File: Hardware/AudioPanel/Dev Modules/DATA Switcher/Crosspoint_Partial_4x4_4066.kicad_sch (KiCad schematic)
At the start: 29 parts, among them U1004 74HC4066BQ, U1005 74HC4066BQ, U1006 74HC4066BQ

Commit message: Many tweaks
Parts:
- removed C49, C50, C51, C53, C54, C55: 100nF, symbol Device:C_Small
- removed C52, C56: 10uF, symbol Device:C_Small
- added C901, C902, C903: 100nF, Capacitor_SMD:C_0402_1005Metric, symbol Device:C_Small
- added C904, C905: 22uF, Capacitor_SMD:C_0603_1608Metric, symbol Device:C_Small
- renumbered D1001 to D901, D1002 to D902, D1003 to D903, D1004 to D904, D1005 to D905, D1006 to D906, D1007 to D907, D1008 to D908, D1009 to D909, D210 to D910, D211 to D911, D212 to D912, RN201 to RN901, RN202 to RN902, RN203 to RN903, RN204 to RN904, RN205 to RN905, RN207 to RN906, U1004 to U901, U1005 to U902, U1006 to U903
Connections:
- net A1: now also D901.2 (A)
- net A1_T: no longer D901.2 (A)
- net A2: now also D902.2 (A)
- net A2_T: no longer D902.2 (A)
- net A3: now also D903.2 (A)
- net A3_T: no longer D903.2 (A)
- net B0: now also D904.2 (A)
- net B0_T: no longer D904.2 (A)
- net B2: now also D905.2 (A)
- net B2_T: no longer D905.2 (A)
- net B3: now also D906.2 (A)
- net B3_T: no longer D906.2 (A)
- net C0: now also D907.2 (A)
- net C0_T: no longer D907.2 (A)
- net C1: now also D908.2 (A)
- net C1_T: no longer D908.2 (A)
- net C3: now also D909.2 (A)
- net C3_T: no longer D909.2 (A)
- net D0: now also D910.2 (A)
- net D0_T: no longer D910.2 (A)
- net D1: now also D911.2 (A)
- net D1_T: no longer D911.2 (A)
- net D2: now also D912.2 (A)
- net D2_T: no longer D912.2 (A)
- net GND: now also C901.2, C902.2, C903.2, C904.2, C905.2
- net VDD: now also C901.1, C902.1, C903.1, C904.1, C905.1

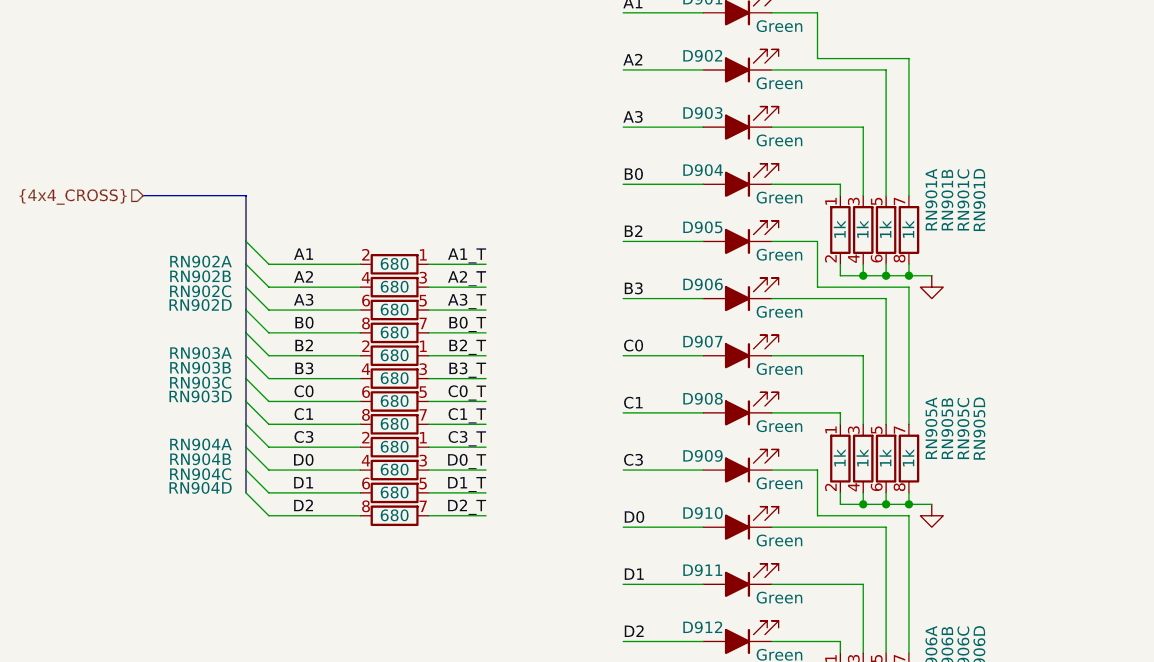
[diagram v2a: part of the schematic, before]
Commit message: Fixed value of RADIO SQUELCH low-pass filter cap
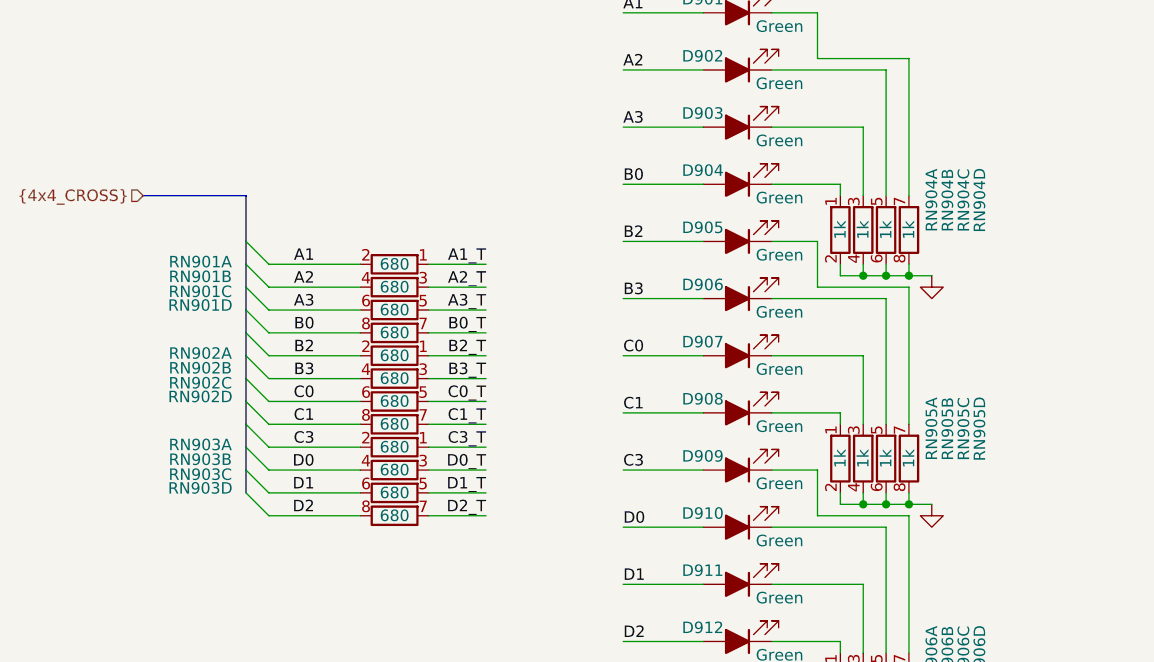
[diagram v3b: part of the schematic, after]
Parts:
- renumbered RN902 to RN901, RN903 to RN902, RN904 to RN903, RN901 to RN904
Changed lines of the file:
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@@
 		(on_board yes)
 		(dnp no)
-		(property "Reference" "RN904"
+		(property "Reference" "RN903"
 			(at 36.83 110.6057 90)
 			(effects
@@
 			(project "DATA Switcher"
 				(path "/f4364825-c4d0-42ed-9bb3-69baf38bc2d0/f5e12c3e-6416-4600-9203-1d5eae1952dd"
-					(reference "RN904")
+					(reference "RN903")
 					(unit 2)
 				)
@@
 		(on_board yes)
 		(dnp no)
-		(property "Reference" "RN902"
+		(property "Reference" "RN901"
 			(at 36.83 93.472 90)
 			(effects
@@
 			(project "DATA Switcher"
 				(path "/f4364825-c4d0-42ed-9bb3-69baf38bc2d0/f5e12c3e-6416-4600-9203-1d5eae1952dd"
-					(reference "RN902")
+					(reference "RN901")
 					(unit 4)
 				)
@@
 		(on_board yes)
 		(dnp no)
-		(property "Reference" "RN901"
+		(property "Reference" "RN904"
 			(at 123.444 81.788 90)
 			(effects
@@
 			(project "DATA Switcher"
 				(path "/f4364825-c4d0-42ed-9bb3-69baf38bc2d0/f5e12c3e-6416-4600-9203-1d5eae1952dd"
-					(reference "RN901")
+					(reference "RN904")
 					(unit 4)
 				)
@@
 		(on_board yes)
 		(dnp no)
-		(property "Reference" "RN901"
+		(property "Reference" "RN904"
 			(at 121.666 81.788 90)
 			(effects
@@
 			(project "DATA Switcher"
 				(path "/f4364825-c4d0-42ed-9bb3-69baf38bc2d0/f5e12c3e-6416-4600-9203-1d5eae1952dd"
-					(reference "RN901")
+					(reference "RN904")
 					(unit 3)
 				)
@@
 		(on_board yes)
 		(dnp no)
-		(property "Reference" "RN901"
+		(property "Reference" "RN904"
 			(at 118.11 81.788 90)
 			(effects
@@
 			(project "DATA Switcher"
 				(path "/f4364825-c4d0-42ed-9bb3-69baf38bc2d0/f5e12c3e-6416-4600-9203-1d5eae1952dd"
-					(reference "RN901")
+					(reference "RN904")
 					(unit 1)
 				)
@@
 		(on_board yes)
 		(dnp no)
-		(property "Reference" "RN903"
+		(property "Reference" "RN902"
 			(at 36.83 98.806 90)
 			(effects
@@
 			(project "DATA Switcher"
 				(path "/f4364825-c4d0-42ed-9bb3-69baf38bc2d0/f5e12c3e-6416-4600-9203-1d5eae1952dd"
-					(reference "RN903")
+					(reference "RN902")
 					(unit 1)
 				)
@@
 		(on_board yes)
 		(dnp no)
-		(property "Reference" "RN901"
+		(property "Reference" "RN904"
 			(at 119.888 81.788 90)
 			(effects
@@
 			(project "DATA Switcher"
 				(path "/f4364825-c4d0-42ed-9bb3-69baf38bc2d0/f5e12c3e-6416-4600-9203-1d5eae1952dd"
-					(reference "RN901")
+					(reference "RN904")
 					(unit 2)
 				)
@@
 		(on_board yes)
 		(dnp no)
-		(property "Reference" "RN903"
+		(property "Reference" "RN902"
 			(at 36.83 102.108 90)
 			(effects
@@
 			(project "DATA Switcher"
 				(path "/f4364825-c4d0-42ed-9bb3-69baf38bc2d0/f5e12c3e-6416-4600-9203-1d5eae1952dd"
-					(reference "RN903")
+					(reference "RN902")
 					(unit 3)
 				)
@@
 		(on_board yes)
 		(dnp no)
-		(property "Reference" "RN904"
+		(property "Reference" "RN903"
 			(at 36.83 113.792 90)
 			(effects
@@
 			(project "DATA Switcher"
 				(path "/f4364825-c4d0-42ed-9bb3-69baf38bc2d0/f5e12c3e-6416-4600-9203-1d5eae1952dd"
-					(reference "RN904")
+					(reference "RN903")
 					(unit 4)
 				)
@@
 		(on_board yes)
 		(dnp no)
-		(property "Reference" "RN903"
+		(property "Reference" "RN902"
 			(at 36.83 103.632 90)
 			(effects
@@
 			(project "DATA Switcher"
 				(path "/f4364825-c4d0-42ed-9bb3-69baf38bc2d0/f5e12c3e-6416-4600-9203-1d5eae1952dd"
-					(reference "RN903")
+					(reference "RN902")
 					(unit 4)
 				)
@@
 		(on_board yes)
 		(dnp no)
-		(property "Reference" "RN902"
+		(property "Reference" "RN901"
 			(at 36.83 91.948 90)
 			(effects
@@
 			(project "DATA Switcher"
 				(path "/f4364825-c4d0-42ed-9bb3-69baf38bc2d0/f5e12c3e-6416-4600-9203-1d5eae1952dd"
-					(reference "RN902")
+					(reference "RN901")
 					(unit 3)
 				)
@@
 		(on_board yes)
 		(dnp no)
-		(property "Reference" "RN902"
+		(property "Reference" "RN901"
 			(at 36.83 90.2857 90)
 			(effects
@@
 			(project "DATA Switcher"
 				(path "/f4364825-c4d0-42ed-9bb3-69baf38bc2d0/f5e12c3e-6416-4600-9203-1d5eae1952dd"
-					(reference "RN902")
+					(reference "RN901")
 					(unit 2)
 				)
@@
 		(on_board yes)
 		(dnp no)
-		(property "Reference" "RN904"
+		(property "Reference" "RN903"
 			(at 36.83 112.268 90)
 			(effects
@@
 			(project "DATA Switcher"
 				(path "/f4364825-c4d0-42ed-9bb3-69baf38bc2d0/f5e12c3e-6416-4600-9203-1d5eae1952dd"
-					(reference "RN904")
+					(reference "RN903")
 					(unit 3)
 				)
@@
 		(on_board yes)
 		(dnp no)
-		(property "Reference" "RN903"
+		(property "Reference" "RN902"
 			(at 36.83 100.4457 90)
 			(effects
@@
 			(project "DATA Switcher"
 				(path "/f4364825-c4d0-42ed-9bb3-69baf38bc2d0/f5e12c3e-6416-4600-9203-1d5eae1952dd"
-					(reference "RN903")
+					(reference "RN902")
 					(unit 2)
 				)
@@
 		(on_board yes)
 		(dnp no)
-		(property "Reference" "RN904"
+		(property "Reference" "RN903"
 			(at 36.83 108.966 90)
 			(effects
@@
 			(project "DATA Switcher"
 				(path "/f4364825-c4d0-42ed-9bb3-69baf38bc2d0/f5e12c3e-6416-4600-9203-1d5eae1952dd"
-					(reference "RN904")
+					(reference "RN903")
 					(unit 1)
 				)
@@
 		(on_board yes)
 		(dnp no)
-		(property "Reference" "RN902"
+		(property "Reference" "RN901"
 			(at 36.83 88.646 90)
 			(effects
@@
 			(project "DATA Switcher"
 				(path "/f4364825-c4d0-42ed-9bb3-69baf38bc2d0/f5e12c3e-6416-4600-9203-1d5eae1952dd"
-					(reference "RN902")
+					(reference "RN901")
 					(unit 1)
 				)

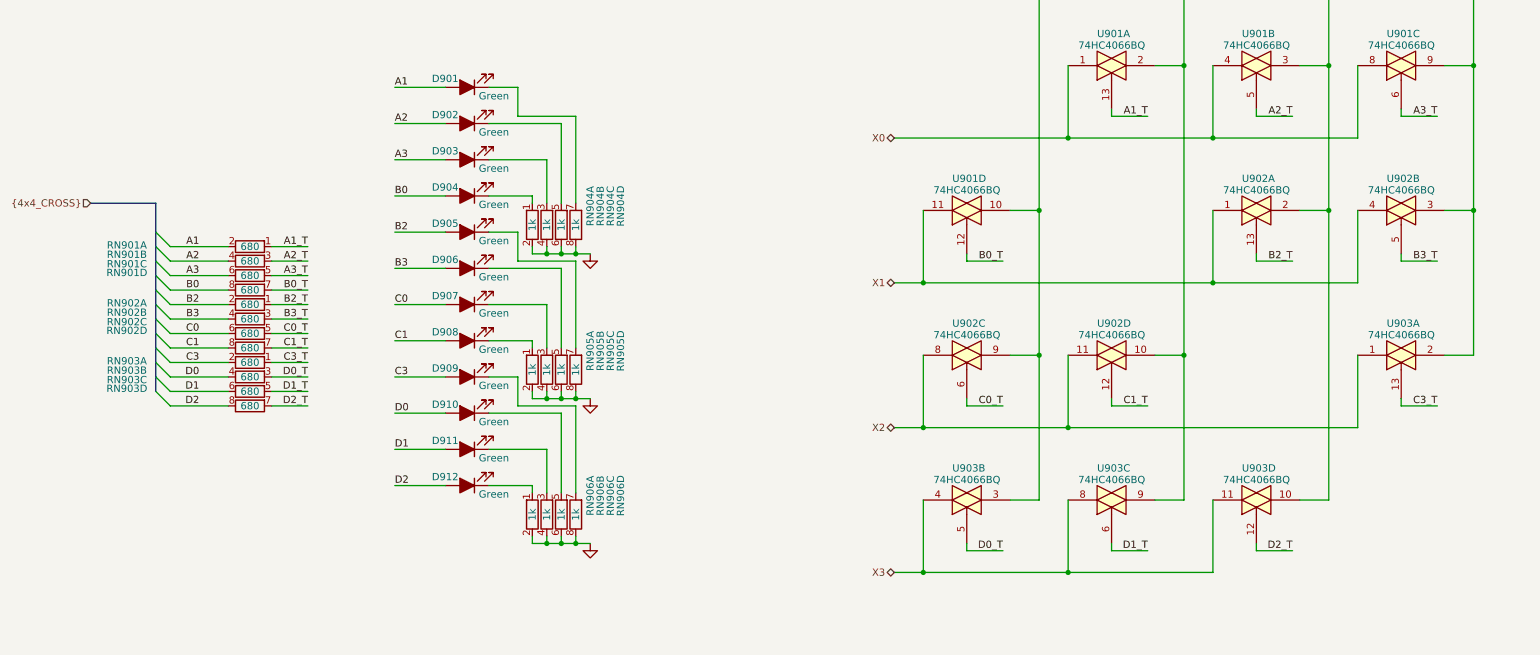
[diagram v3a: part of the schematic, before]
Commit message: Fixed I2C pullups to 3V3
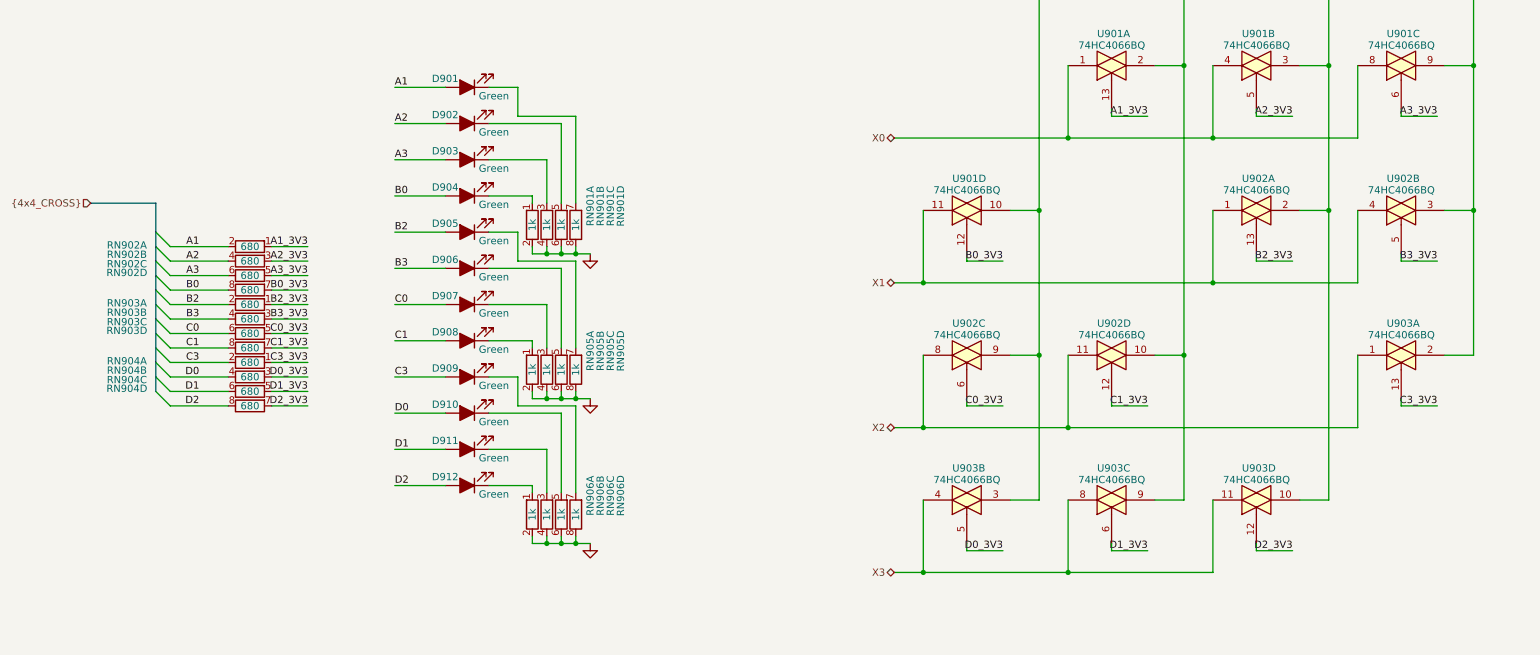
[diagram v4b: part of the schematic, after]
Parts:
- renumbered RN904 to RN901, RN901 to RN902, RN902 to RN903, RN903 to RN904
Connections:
- net A1_T renamed A1_3V3
- net A2_T renamed A2_3V3
- net A3_T renamed A3_3V3
- net B0_T renamed B0_3V3
- net B2_T renamed B2_3V3
- net B3_T renamed B3_3V3
- net C0_T renamed C0_3V3
- net C1_T renamed C1_3V3
- net C3_T renamed C3_3V3
- net D0_T renamed D0_3V3
- net D1_T renamed D1_3V3
- net D2_T renamed D2_3V3
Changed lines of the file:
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@@
 		)
 	)
-	(label "D0_T"
+	(label "D0_3V3"
 		(at 190.5 142.24 180)
 		(effects
@@
 		)
 	)
-	(label "C0_T"
+	(label "C0_3V3"
 		(at 190.5 116.84 180)
 		(effects
@@
 		)
 	)
-	(label "D1_T"
+	(label "D1_3V3"
 		(at 68.58 114.3 180)
 		(effects
@@
 		)
 	)
-	(label "C3_T"
+	(label "C3_3V3"
 		(at 68.58 109.22 180)
 		(effects
@@
 		)
 	)
-	(label "A3_T"
+	(label "A3_3V3"
 		(at 68.58 93.98 180)
 		(effects
@@
 		)
 	)
-	(label "C0_T"
+	(label "C0_3V3"
 		(at 68.58 104.14 180)
 		(effects
@@
 		)
 	)
-	(label "D0_T"
+	(label "D0_3V3"
 		(at 68.58 111.76 180)
 		(effects
@@
 		)
 	)
-	(label "D1_T"
+	(label "D1_3V3"
 		(at 215.9 142.24 180)
 		(effects
@@
 		)
 	)
-	(label "C3_T"
+	(label "C3_3V3"
 		(at 266.7 116.84 180)
 		(effects
@@
 		)
 	)
-	(label "C1_T"
+	(label "C1_3V3"
 		(at 68.58 106.68 180)
 		(effects
@@
 		)
 	)
-	(label "B2_T"
+	(label "B2_3V3"
 		(at 241.3 91.44 180)
 		(effects
@@
 		)
 	)
-	(label "B0_T"
+	(label "B0_3V3"
 		(at 68.58 96.52 180)
 		(effects
@@
 		)
 	)
-	(label "B3_T"
+	(label "B3_3V3"
 		(at 68.58 101.6 180)
 		(effects
@@
 		)
 	)
-	(label "A2_T"
+	(label "A2_3V3"
 		(at 241.3 66.04 180)
 		(effects
@@
 		)
 	)
-	(label "A1_T"
+	(label "A1_3V3"
 		(at 215.9 66.04 180)
 		(effects
@@
 		)
 	)
-	(label "D2_T"
+	(label "D2_3V3"
 		(at 68.58 116.84 180)
 		(effects
@@
 		)
 	)
-	(label "B0_T"
+	(label "B0_3V3"
 		(at 190.5 91.44 180)
 		(effects
@@
 		)
 	)
-	(label "D2_T"
+	(label "D2_3V3"
 		(at 241.3 142.24 180)
 		(effects
@@
 		)
 	)
-	(label "A2_T"
+	(label "A2_3V3"
 		(at 68.58 91.44 180)
 		(effects
@@
 		)
 	)
-	(label "A3_T"
+	(label "A3_3V3"
 		(at 266.7 66.04 180)
 		(effects
@@
 		)
 	)
-	(label "B2_T"
+	(label "B2_3V3"
 		(at 68.58 99.06 180)
 		(effects
@@
 		)
 	)
-	(label "A1_T"
+	(label "A1_3V3"
 		(at 68.58 88.9 180)
 		(effects
@@
 		)
 	)
-	(label "C1_T"
+	(label "C1_3V3"
 		(at 215.9 116.84 180)
 		(effects
@@
 		)
 	)
-	(label "B3_T"
+	(label "B3_3V3"
 		(at 266.7 91.44 180)
 		(effects
@@
 		(on_board yes)
 		(dnp no)
-		(property "Reference" "RN903"
+		(property "Reference" "RN904"
 			(at 36.83 110.6057 90)
 			(effects
@@
 			(project "DATA Switcher"
 				(path "/f4364825-c4d0-42ed-9bb3-69baf38bc2d0/f5e12c3e-6416-4600-9203-1d5eae1952dd"
-					(reference "RN903")
+					(reference "RN904")
 					(unit 2)
 				)
@@
 		(on_board yes)
 		(dnp no)
-		(property "Reference" "RN901"
+		(property "Reference" "RN902"
 			(at 36.83 93.472 90)
 			(effects
@@
 			(project "DATA Switcher"
 				(path "/f4364825-c4d0-42ed-9bb3-69baf38bc2d0/f5e12c3e-6416-4600-9203-1d5eae1952dd"
-					(reference "RN901")
+					(reference "RN902")
 					(unit 4)
 				)
@@
 		(on_board yes)
 		(dnp no)
-		(property "Reference" "RN904"
+		(property "Reference" "RN901"
 			(at 123.444 81.788 90)
 			(effects
@@
 			(project "DATA Switcher"
 				(path "/f4364825-c4d0-42ed-9bb3-69baf38bc2d0/f5e12c3e-6416-4600-9203-1d5eae1952dd"
-					(reference "RN904")
+					(reference "RN901")
 					(unit 4)
 				)
@@
 		(on_board yes)
 		(dnp no)
-		(property "Reference" "RN904"
+		(property "Reference" "RN901"
 			(at 121.666 81.788 90)
 			(effects
@@
 			(project "DATA Switcher"
 				(path "/f4364825-c4d0-42ed-9bb3-69baf38bc2d0/f5e12c3e-6416-4600-9203-1d5eae1952dd"
-					(reference "RN904")
+					(reference "RN901")
 					(unit 3)
 				)
@@
 		(on_board yes)
 		(dnp no)
-		(property "Reference" "RN904"
+		(property "Reference" "RN901"
 			(at 118.11 81.788 90)
 			(effects
@@
 			(project "DATA Switcher"
 				(path "/f4364825-c4d0-42ed-9bb3-69baf38bc2d0/f5e12c3e-6416-4600-9203-1d5eae1952dd"
-					(reference "RN904")
+					(reference "RN901")
 					(unit 1)
 				)
@@
 		(on_board yes)
 		(dnp no)
-		(property "Reference" "RN902"
+		(property "Reference" "RN903"
 			(at 36.83 98.806 90)
 			(effects
@@
 			(project "DATA Switcher"
 				(path "/f4364825-c4d0-42ed-9bb3-69baf38bc2d0/f5e12c3e-6416-4600-9203-1d5eae1952dd"
-					(reference "RN902")
+					(reference "RN903")
 					(unit 1)
 				)
@@
 		(on_board yes)
 		(dnp no)
-		(property "Reference" "RN904"
+		(property "Reference" "RN901"
 			(at 119.888 81.788 90)
 			(effects
@@
 			(project "DATA Switcher"
 				(path "/f4364825-c4d0-42ed-9bb3-69baf38bc2d0/f5e12c3e-6416-4600-9203-1d5eae1952dd"
-					(reference "RN904")
+					(reference "RN901")
 					(unit 2)
 				)
@@
 		(on_board yes)
 		(dnp no)
-		(property "Reference" "RN902"
+		(property "Reference" "RN903"
 			(at 36.83 102.108 90)
 			(effects
@@
 			(project "DATA Switcher"
 				(path "/f4364825-c4d0-42ed-9bb3-69baf38bc2d0/f5e12c3e-6416-4600-9203-1d5eae1952dd"
-					(reference "RN902")
+					(reference "RN903")
 					(unit 3)
 				)
@@
 		(on_board yes)
 		(dnp no)
-		(property "Reference" "RN903"
+		(property "Reference" "RN904"
 			(at 36.83 113.792 90)
 			(effects
@@
 			(project "DATA Switcher"
 				(path "/f4364825-c4d0-42ed-9bb3-69baf38bc2d0/f5e12c3e-6416-4600-9203-1d5eae1952dd"
-					(reference "RN903")
+					(reference "RN904")
 					(unit 4)
 				)
@@
 		(on_board yes)
 		(dnp no)
-		(property "Reference" "RN902"
+		(property "Reference" "RN903"
 			(at 36.83 103.632 90)
 			(effects
@@
 			(project "DATA Switcher"
 				(path "/f4364825-c4d0-42ed-9bb3-69baf38bc2d0/f5e12c3e-6416-4600-9203-1d5eae1952dd"
-					(reference "RN902")
+					(reference "RN903")
 					(unit 4)
 				)
@@
 		(on_board yes)
 		(dnp no)
-		(property "Reference" "RN901"
+		(property "Reference" "RN902"
 			(at 36.83 91.948 90)
 			(effects
@@
 			(project "DATA Switcher"
 				(path "/f4364825-c4d0-42ed-9bb3-69baf38bc2d0/f5e12c3e-6416-4600-9203-1d5eae1952dd"
-					(reference "RN901")
+					(reference "RN902")
 					(unit 3)
 				)
@@
 		(on_board yes)
 		(dnp no)
-		(property "Reference" "RN901"
+		(property "Reference" "RN902"
 			(at 36.83 90.2857 90)
 			(effects
@@
 			(project "DATA Switcher"
 				(path "/f4364825-c4d0-42ed-9bb3-69baf38bc2d0/f5e12c3e-6416-4600-9203-1d5eae1952dd"
-					(reference "RN901")
+					(reference "RN902")
 					(unit 2)
 				)
@@
 		(on_board yes)
 		(dnp no)
-		(property "Reference" "RN903"
+		(property "Reference" "RN904"
 			(at 36.83 112.268 90)
 			(effects
@@
 			(project "DATA Switcher"
 				(path "/f4364825-c4d0-42ed-9bb3-69baf38bc2d0/f5e12c3e-6416-4600-9203-1d5eae1952dd"
-					(reference "RN903")
+					(reference "RN904")
 					(unit 3)
 				)
@@
 		(on_board yes)
 		(dnp no)
-		(property "Reference" "RN902"
+		(property "Reference" "RN903"
 			(at 36.83 100.4457 90)
 			(effects
@@
 			(project "DATA Switcher"
 				(path "/f4364825-c4d0-42ed-9bb3-69baf38bc2d0/f5e12c3e-6416-4600-9203-1d5eae1952dd"
-					(reference "RN902")
+					(reference "RN903")
 					(unit 2)
 				)
@@
 		(on_board yes)
 		(dnp no)
-		(property "Reference" "RN903"
+		(property "Reference" "RN904"
 			(at 36.83 108.966 90)
 			(effects
@@
 			(project "DATA Switcher"
 				(path "/f4364825-c4d0-42ed-9bb3-69baf38bc2d0/f5e12c3e-6416-4600-9203-1d5eae1952dd"
-					(reference "RN903")
+					(reference "RN904")
 					(unit 1)
 				)
@@
 		(on_board yes)
 		(dnp no)
-		(property "Reference" "RN901"
+		(property "Reference" "RN902"
 			(at 36.83 88.646 90)
 			(effects
@@
 			(project "DATA Switcher"
 				(path "/f4364825-c4d0-42ed-9bb3-69baf38bc2d0/f5e12c3e-6416-4600-9203-1d5eae1952dd"
-					(reference "RN901")
+					(reference "RN902")
 					(unit 1)
 				)

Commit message: Changed passives to Worthingtons
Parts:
- C901, C902, C903: footprint Capacitor_SMD:C_0402_1005Metric -> Libraries:Worthington_C_0402
- C904, C905: footprint Capacitor_SMD:C_0603_1608Metric -> Libraries:Worthington_C_0603
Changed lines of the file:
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@@
 			)
 		)
-		(property "Footprint" "Capacitor_SMD:C_0402_1005Metric"
+		(property "Footprint" "Libraries:Worthington_C_0402"
 			(at 271.78 175.26 0)
 			(effects
@@
 			)
 		)
-		(property "Footprint" "Capacitor_SMD:C_0603_1608Metric"
+		(property "Footprint" "Libraries:Worthington_C_0603"
 			(at 311.15 175.26 0)
 			(effects
@@
 			)
 		)
-		(property "Footprint" "Capacitor_SMD:C_0402_1005Metric"
+		(property "Footprint" "Libraries:Worthington_C_0402"
 			(at 297.18 175.26 0)
 			(effects
@@
 			)
 		)
-		(property "Footprint" "Capacitor_SMD:C_0603_1608Metric"
+		(property "Footprint" "Libraries:Worthington_C_0603"
 			(at 325.12 175.26 0)
 			(effects
@@
 			)
 		)
-		(property "Footprint" "Capacitor_SMD:C_0402_1005Metric"
+		(property "Footprint" "Libraries:Worthington_C_0402"
 			(at 284.48 175.26 0)
 			(effects
